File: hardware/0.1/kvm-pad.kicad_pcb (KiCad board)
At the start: 2 copper layers, 76.2 x 64.1 mm, 93 parts, among them J1 USB_C_Receptacle_USB2.0, J2 USB_C_Receptacle_USB2.0, J3 AVR-ISP-6, J4 USB_A, J5 USB_A, J6 USB_A, K1 KEYSW, K2 KEYSW, K3 KEYSW, K4 KEYSW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

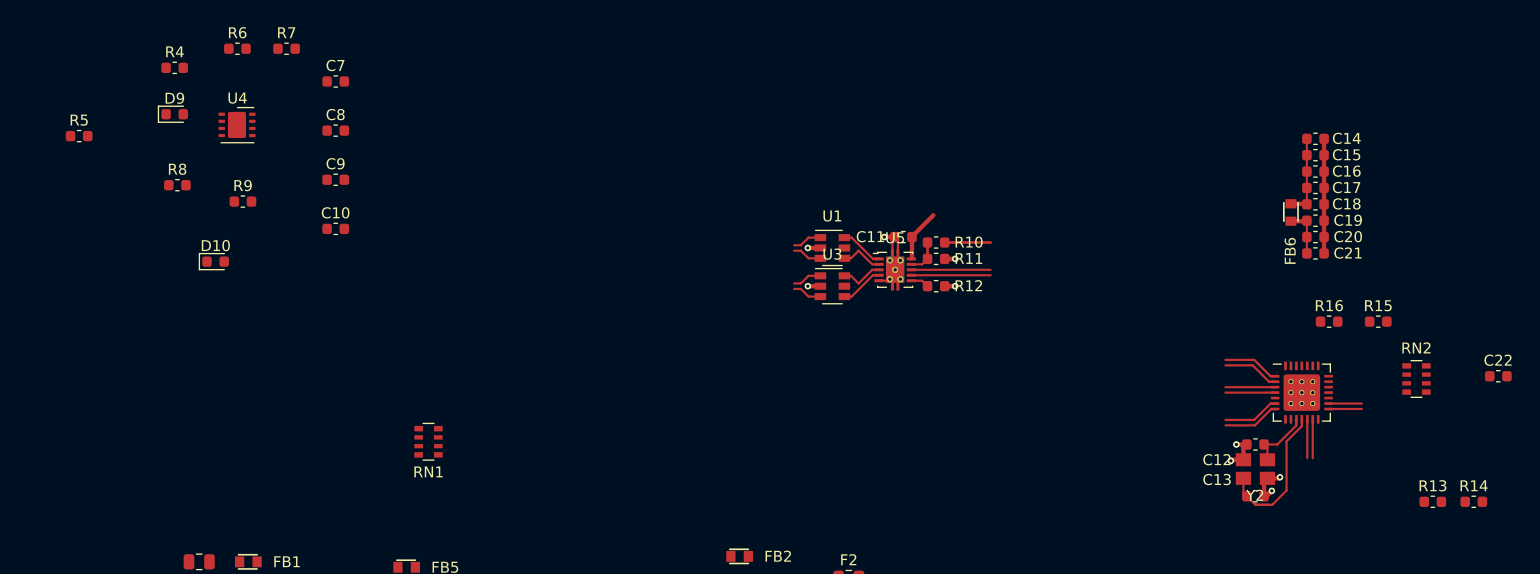
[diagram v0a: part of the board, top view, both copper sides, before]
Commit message: [pcb] Power switch routing
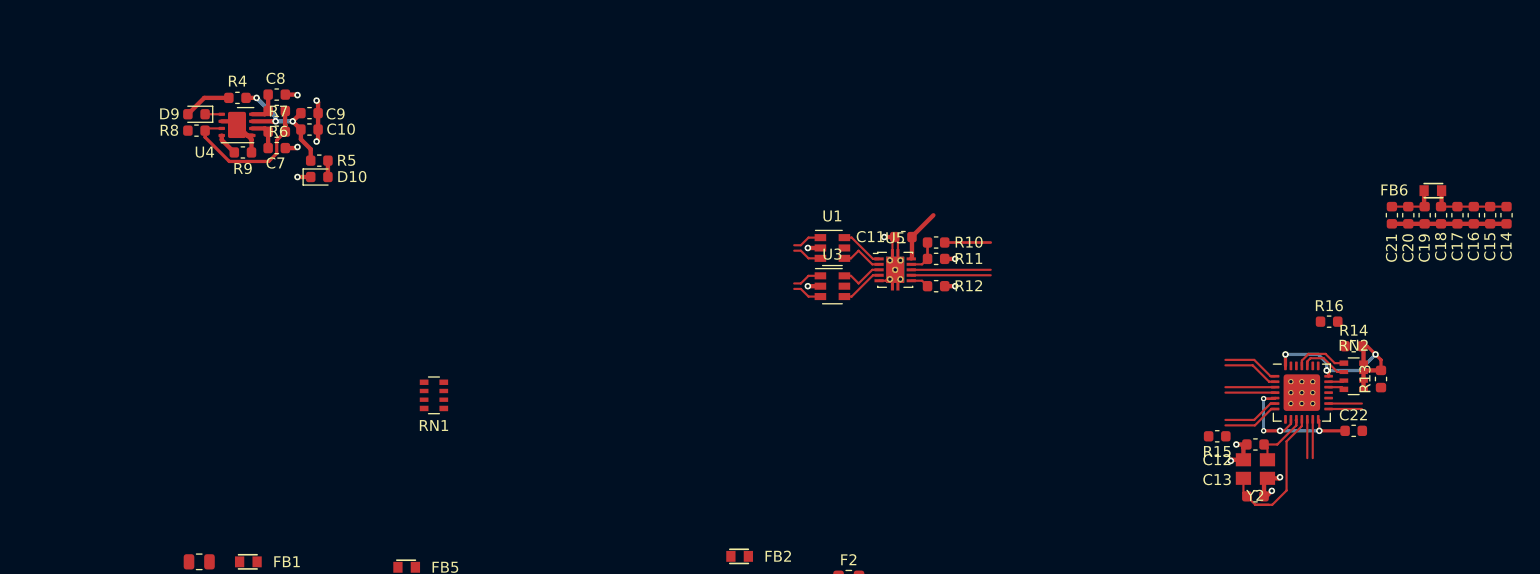
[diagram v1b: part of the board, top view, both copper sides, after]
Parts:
- moved R5 22.1 mm to (27.0, -41.8)
- moved C14 18.8 mm to (135.8, -36.8), turned to 270 degrees
- moved R15 18.1 mm to (109.2, -16.5), turned to 180 degrees
- moved R14 18.0 mm to (121.8, -24.8)
- moved C15 16.9 mm to (134.2, -36.8), turned to 270 degrees
- moved C16 15.0 mm to (132.8, -36.8), turned to 270 degrees
- moved C22 14.2 mm to (121.8, -17.0)
- moved C17 13.2 mm to (131.2, -36.8), turned to 270 degrees
- moved FB6 13.2 mm to (129.0, -39.0), turned to 180 degrees
- moved D10 12.3 mm to (27.0, -40.2)
- moved R13 12.2 mm to (124.2, -21.8), turned to 90 degrees
- moved C18 11.5 mm to (129.8, -36.8), turned to 270 degrees
- moved C19 10.0 mm to (128.2, -36.8), turned to 270 degrees
- moved C10 9.41 mm to (26.1, -44.6)
- moved C20 8.73 mm to (126.8, -36.8), turned to 270 degrees
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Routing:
- net +3V3: track 4.48 -> 24.9 mm, vias 0 -> 3
- net +3.3VA: track 12.3 -> 26.6 mm, vias 0 -> 4
- net Net-(R6-Pad1): track 0.00 -> 14.2 mm
- net +5V: track 3.00 -> 15.9 mm, vias 0 -> 3
- net GND: track 31.4 -> 43.8 mm, vias 9 -> 14
- net /usb/nOVR_1: track 0.00 -> 4.94 mm
- net /usb/nOVR_2: track 0.00 -> 4.40 mm
- net Net-(D9-Pad2): track 0.00 -> 4.37 mm
- net /USB_5V_2: track 0.00 -> 3.07 mm
- net /USB_5V_1: track 0.00 -> 3.07 mm
- net Net-(R9-Pad1): track 0.00 -> 2.03 mm
- net Net-(D9-Pad1): track 0.00 -> 1.52 mm
- net Net-(D10-Pad2): track 0.00 -> 1.50 mm
- net /usb/nOVR_4: track 0.00 -> 1.48 mm
- net /usb/nOVR_3: track 0.00 -> 1.44 mm

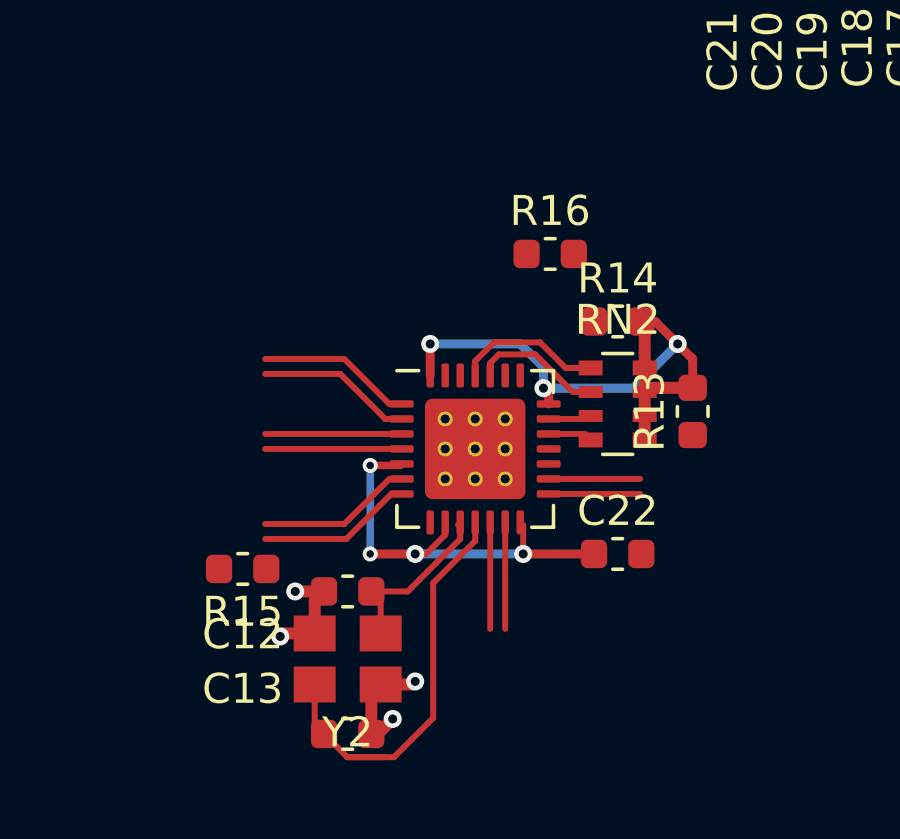
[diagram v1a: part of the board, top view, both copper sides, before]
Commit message: [pcb] Hub routing
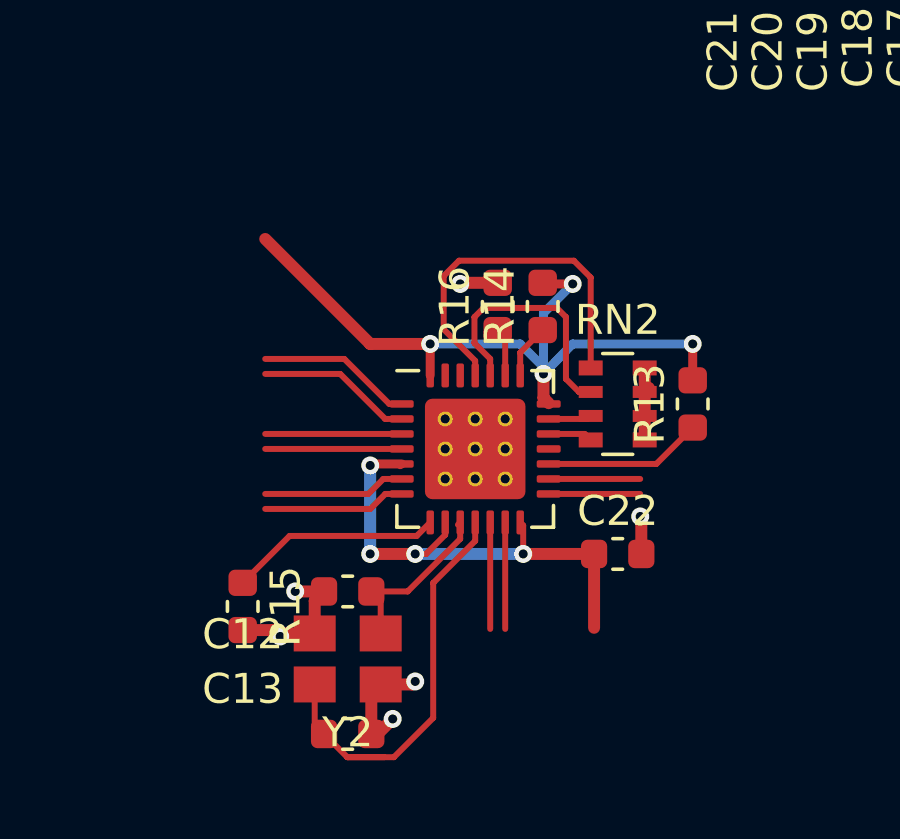
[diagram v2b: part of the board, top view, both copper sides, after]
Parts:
- moved R14 2.55 mm to (119.2, -25.2), turned to 90 degrees
- moved R16 2.47 mm to (117.8, -25.2), turned to 90 degrees
- moved R15 1.25 mm to (109.2, -15.2), turned to 270 degrees
- moved R13 0.25 mm to (124.2, -22.0)
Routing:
- net /usb/nOVR_1: track 4.94 -> 12.1 mm
- net Net-(R15-Pad1): track 0.00 -> 7.08 mm
- net +3V3: track 24.9 -> 31.2 mm, vias 3 -> 4
- net Net-(R13-Pad1): track 0.00 -> 5.30 mm
- net /usb/nOVR_2: track 4.40 -> 8.53 mm
- net GND: track 43.8 -> 47.7 mm, vias 14 -> 16
- net +3.3VA: track 26.6 -> 29.1 mm
- net Net-(R14-Pad1): track 0.00 -> 1.82 mm
- net Net-(R16-Pad1): track 0.00 -> 1.62 mm

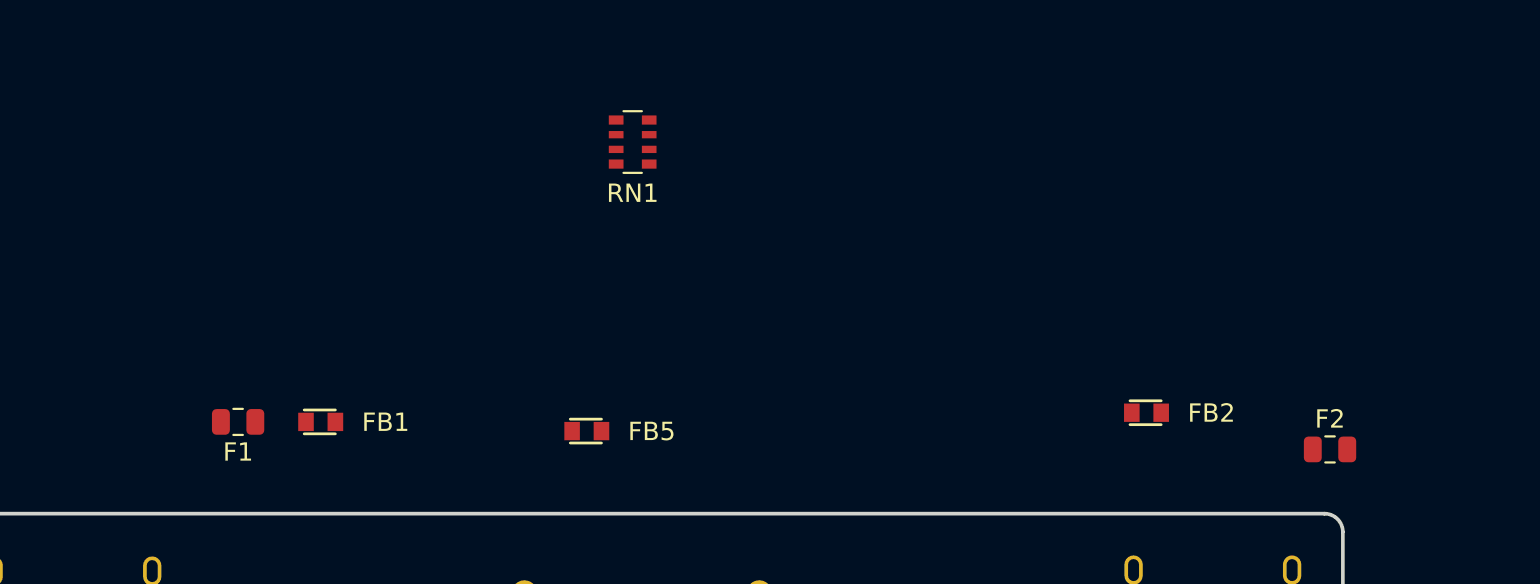
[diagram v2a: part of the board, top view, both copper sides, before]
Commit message: [pcb] Switch RN1 to 4xR
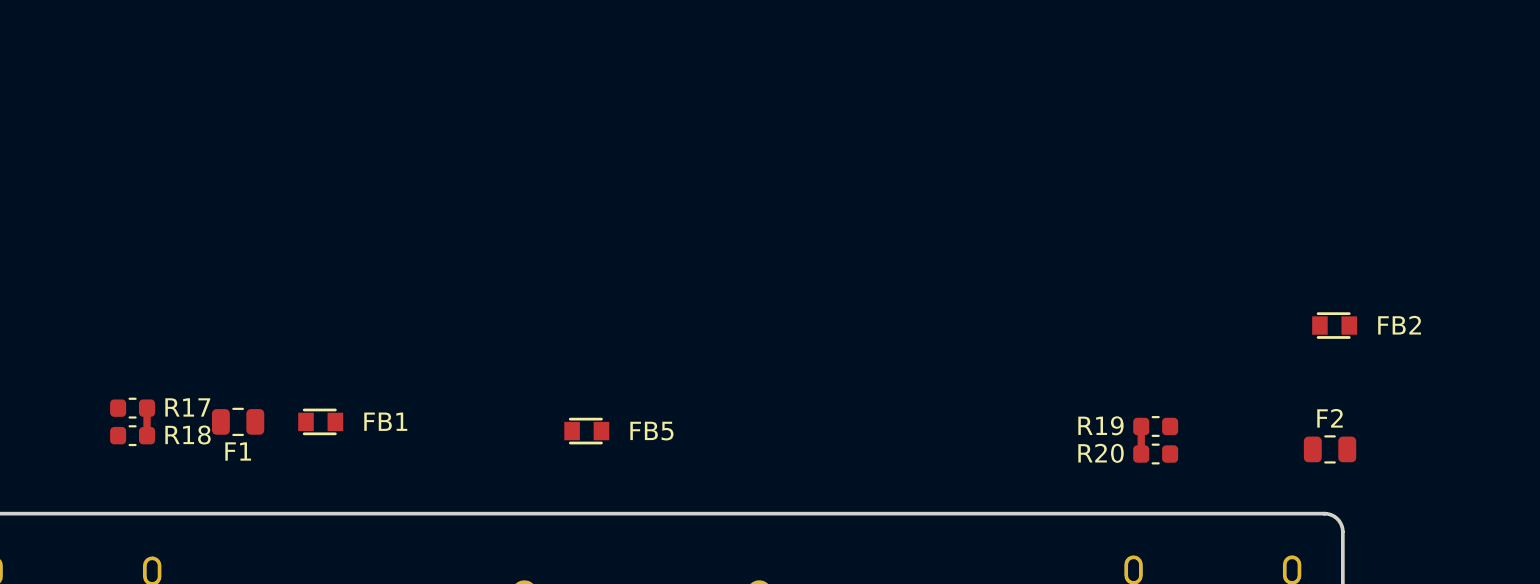
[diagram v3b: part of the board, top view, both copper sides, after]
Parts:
- added R18: 5K1, Resistor_SMD:R_0603_1608Metric, F.Cu at (10.2, -4.25)
- added R19: 5K1, Resistor_SMD:R_0603_1608Metric, F.Cu at (66.0, -4.75)
- added R20: 5K1, Resistor_SMD:R_0603_1608Metric, F.Cu at (66.0, -3.25)
- R17: renamed from RN1; footprint Resistor_SMD:R_Array_Convex_4x0603 -> Resistor_SMD:R_0603_1608Metric
- moved R17 30.9 mm to (10.2, -5.75)
- moved FB2 11.3 mm to (75.8, -10.2)
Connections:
- R17 pad 1: Net-(J2-PadB5) -> GND
- R17 pad 2: Net-(J2-PadA5) -> Net-(J1-PadA5)
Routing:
- net GND: track 47.7 -> 50.7 mm

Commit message: [pcb] Small edits
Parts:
- moved C10 20.8 mm to (14.8, -27.1)
- moved C7 20.8 mm to (11.8, -25.4)
- moved C9 20.8 mm to (14.8, -28.6)
- moved D10 20.8 mm to (15.8, -22.8)
- moved D9 20.8 mm to (4.50, -28.5)
- moved R4 20.8 mm to (8.25, -30.0)
- moved R5 20.8 mm to (15.8, -24.2)
- moved R6 20.8 mm to (11.8, -26.9)
- moved R8 20.8 mm to (4.50, -27.0)
- moved R9 20.8 mm to (8.75, -25.0)
- moved U4 20.8 mm to (8.25, -27.5)
- moved C8 20.8 mm to (11.8, -30.3)
- moved R7 20.8 mm to (11.8, -28.8)

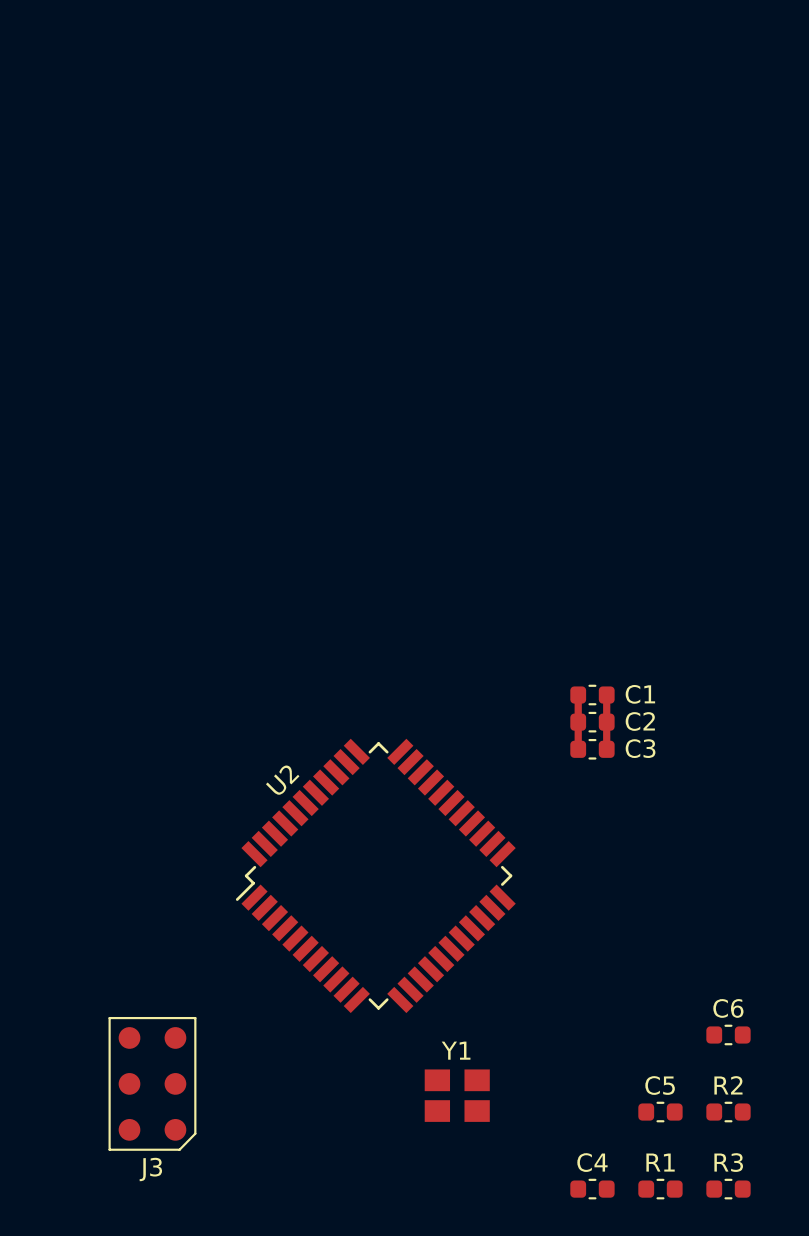
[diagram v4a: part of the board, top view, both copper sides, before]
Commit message: [pcb] MCU routing
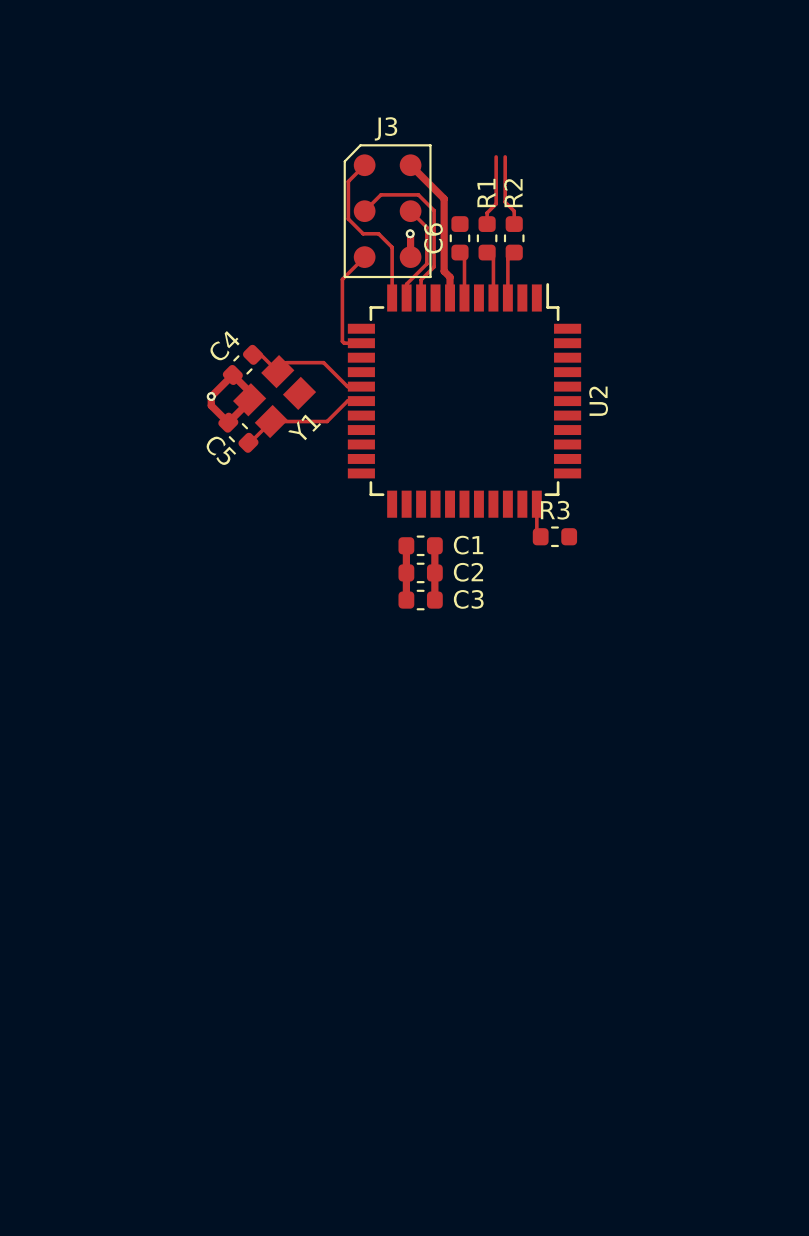
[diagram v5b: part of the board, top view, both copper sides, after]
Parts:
- moved R1 53.4 mm to (121.0, 33.8), turned to 90 degrees
- moved J3 50.0 mm to (115.5, 32.2), turned to 270 degrees
- moved R2 49.7 mm to (122.5, 33.8), turned to 90 degrees
- moved C4 49.5 mm to (107.5, 40.8), turned to 225 degrees
- moved C6 46.5 mm to (119.5, 33.8), turned to 90 degrees
- moved C5 44.2 mm to (107.2, 44.5), turned to 135 degrees
- moved Y1 39.9 mm to (109.2, 42.5), turned to 225 degrees
- moved R3 37.3 mm to (124.8, 50.2)
- moved U2 26.7 mm to (119.8, 42.8), turned to 270 degrees
- moved C1 12.6 mm to (117.3, 50.8)
- moved C2 12.6 mm to (117.3, 52.2)
- moved C3 12.6 mm to (117.3, 53.8)
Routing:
- net /SCK: track 0.00 -> 9.70 mm
- net /MISO: track 0.00 -> 9.21 mm
- net GND: track 50.7 -> 59.0 mm, vias 16 -> 18
- net +5V: track 15.9 -> 24.1 mm
- net Net-(C5-Pad1): track 0.00 -> 7.20 mm
- net Net-(C4-Pad1): track 0.00 -> 7.13 mm
- net /nRST: track 0.00 -> 6.26 mm
- net /MOSI: track 0.00 -> 5.64 mm
- net /MCU_D-: track 3.05 -> 6.97 mm
- net /MCU_D+: track 3.05 -> 6.97 mm
- net Net-(R2-Pad1): track 0.00 -> 2.66 mm
- net Net-(R1-Pad1): track 0.00 -> 2.66 mm
- net Net-(C6-Pad1): track 0.00 -> 2.62 mm
- net Net-(R3-Pad1): track 0.00 -> 1.89 mm

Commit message: [pcb] More routing
Also add a GND plane on bottom
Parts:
- moved LOGO1 108.1 mm to (-19.0, -16.0)
- moved FB6 35.0 mm to (111.0, -9.00), turned to 270 degrees
- moved C21 33.7 mm to (113.2, -5.25), turned to 0 degrees
- moved C20 32.9 mm to (113.2, -6.75), turned to 0 degrees
- moved C19 32.2 mm to (113.2, -8.25), turned to 0 degrees
- moved C18 31.6 mm to (113.2, -9.75), turned to 0 degrees
- moved C17 31.2 mm to (113.2, -11.2), turned to 0 degrees
- moved C16 30.9 mm to (113.2, -12.8), turned to 0 degrees
- moved C14 30.8 mm to (113.2, -15.8), turned to 0 degrees
- moved C15 30.8 mm to (113.2, -14.2), turned to 0 degrees
- moved D20 22.1 mm to (-7.25, 25.5)
- moved C1 19.6 mm to (98.8, 44.2)
- moved C2 19.6 mm to (98.8, 45.8)
- moved C3 19.6 mm to (98.8, 47.2)
- moved C4 19.6 mm to (89.0, 34.2)
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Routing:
- net +3V3: track 31.2 -> 33.5 mm
- net GND: track 59.0 -> 60.3 mm, vias 18 -> 19
- net +3.3VA: track 29.1 -> 28.0 mm, vias 4 -> 3
- added copper zone on B.Cu, net GND
